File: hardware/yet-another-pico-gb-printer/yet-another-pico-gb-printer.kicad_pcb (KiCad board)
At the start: 4 copper layers, 61 x 22 mm, 90 parts, among them J1 USB_C_Receptacle_USB2.0, J2 Conn_01x02_Shielded, J3 Micro_SD_Card_Det1, J5 GameBoy_LinkPort, J6 Conn_01x03_MountingPin, J7 Conn_01x04, Q1 DMG3415U, Q2 BSS138, Q3 BSS138, Q4 BSS138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

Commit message: schematics and layout improvements
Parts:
- added C20: 100n, Capacitor_SMD:C_0402_1005Metric, F.Cu at (44.4, 81.8)
- SW2: footprint Bongo-Cat-Fidget-Toy:SW_SKRPACE010 -> yet-another-pico-gb-printer:SW-SMD_4P-L5.2-W5.2-P3.70-LS6.4
- moved Q2 25.1 mm to (42.6, 87.5), turned to -90 degrees
- moved Q3 22.8 mm to (47.8, 87.6), turned to -90 degrees
- moved R30 22.5 mm to (42.6, 84.7), turned to 180 degrees
- moved R21 22.2 mm to (50.4, 87.6), turned to -90 degrees
- moved R20 22.2 mm to (45.1, 87.5), turned to -90 degrees
- moved R22 18.9 mm to (47.8, 84.8), turned to 180 degrees
- moved R46 16.0 mm to (44.1, 98.8)
- moved R47 16.0 mm to (44.1, 101.7)
- moved D2 15.6 mm to (67.0, 74.4)
- moved Q4 15.2 mm to (53.1, 87.7), turned to -90 degrees
- moved R24 14.1 mm to (55.6, 87.7), turned to -90 degrees
- moved R23 11.8 mm to (53.1, 84.9), turned to 180 degrees
- moved SW2 9.22 mm to (67.0, 80.2)
- moved SW5 8.80 mm to (35.7, 88.5)
- moved R14 5.46 mm to (54.2, 72.6)
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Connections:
- SW5 pad 4: unconnected-(SW5-A-Pad4) -> /~{USB_BOOT}
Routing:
- net +3V3: track 29.0 -> 124.3 mm, vias 0 -> 9
- net /GB_SO: track 0.00 -> 36.8 mm
- net /GB_SC: track 0.00 -> 36.7 mm
- net /GB_SI: track 0.00 -> 27.2 mm
- net Net-(SW3-C): track 1.53 -> 24.7 mm, vias 0 -> 1
- net /SPI_1_MISO: track 0.00 -> 12.7 mm, vias 0 -> 1
- net /SPI_1_MOSI: track 0.00 -> 10.9 mm, vias 0 -> 1
- net /GB_SCK: track 0.00 -> 9.46 mm
- net /SPI_1_SCK: track 0.00 -> 8.71 mm, vias 0 -> 1
- net /GB_MOSI: track 0.00 -> 8.46 mm
- net /PUSH_BTN: track 0.00 -> 8.35 mm
- net /SPI_1_CS: track 0.00 -> 7.70 mm, vias 0 -> 1
- net +BATT: track 21.9 -> 29.1 mm
- net /GB_MISO: track 0.00 -> 6.35 mm
- net 3V3: track 0.00 -> 6.00 mm
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
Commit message: schematics and layout improvements
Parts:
- added H1: M2, MountingHole:MountingHole_2.2mm_M2_Pad, F.Cu at (74.8, 71.9)
- added H2: M2, MountingHole:MountingHole_2.2mm_M2_Pad, F.Cu at (74.7, 88.4)
- added H3: M2, MountingHole:MountingHole_2.2mm_M2_Pad, F.Cu at (0.58, 86.9)
- added H4: M2, MountingHole:MountingHole_2.2mm_M2_Pad, F.Cu at (41.8, 88.3)

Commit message: sent to fab
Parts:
- removed H1, H2, H3, H4: M2, MountingHole:MountingHole_2.2mm_M2_Pad
- removed R25: 10k, Resistor_SMD:R_0603_1608Metric
- added R15: 0, Resistor_SMD:R_0402_1005Metric, F.Cu at (68.2, 86.1)
- added R16: 0, Resistor_SMD:R_0402_1005Metric, F.Cu at (68.2, 85.1)
- added R17: 0, Resistor_SMD:R_0402_1005Metric, F.Cu at (68.1, 87.1)
- added R18: 0, Resistor_SMD:R_0402_1005Metric, F.Cu at (68.1, 88.1)
- added R19: 10k, Resistor_SMD:R_0402_1005Metric, F.Cu at (66.0, 85.6)
- J5: footprint Gekkio_Connector:GameBoy_LinkPort_MGB_Horizontal -> yet-another-pico-gb-printer:GBA-LINK
- J6: moved to B.Cu
- R20, R21, R22, R23, R24, R26, R29, R3, R30: footprint Resistor_SMD:R_0603_1608Metric -> Resistor_SMD:R_0402_1005Metric
- SW3: footprint Bongo-Cat-Fidget-Toy:SW-SMD_SK-3245S-L1-A-1 -> yet-another-pico-gb-printer:SW-SMD_K3-1280S-L1
- moved J6 37.2 mm to (62.2, 90.2)
- moved R42 32.3 mm to (64.1, 85.1)
- moved R41 32.3 mm to (64.1, 86.1)
- moved R10 23.2 mm to (41.0, 87.5), turned to 90 degrees
- moved R47 21.8 mm to (56.2, 83.6)
- moved D3 21.3 mm to (39.7, 87.6), turned to 90 degrees
- moved R46 18.3 mm to (56.2, 85.1)
- moved SW3 6.61 mm to (28.1, 74.4), turned to 90 degrees
- moved C25 4.25 mm to (29.6, 84.8), turned to 180 degrees
- moved J5 3.55 mm to (70.5, 80.2), turned to 90 degrees
- moved J3 3.10 mm to (51.6, 85.7)
- moved D2 1.94 mm to (65.0, 74.6), turned to 180 degrees
- moved SW2 1.93 mm to (65.1, 80.1)
- moved SW5 0.98 mm to (35.6, 87.5)
- moved J1 0.92 mm to (19.2, 80.2)
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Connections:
- net Net-(U1-USB_DM) renamed /PICO_USB_D_N
- net Net-(U1-USB_DP) renamed /PICO_USB_D_P
- D2 pad 4: 3V3 -> +3V3
- J5 pad 2: /GB_SO -> Net-(J5-SO)
- J5 pad 3: /GB_SI -> Net-(J5-SI)
- R32 pad 1: Net-(SW3-C) -> Net-(SW3-A)
- R4 pad 1: Net-(SW3-C) -> Net-(SW3-A)
- SW2 pad 3: 3V3 -> +3V3
- SW2 pad 4: 3V3 -> +3V3
- SW3 pad 1: Net-(SW3-C) -> unconnected-(SW3-C-Pad1)
- SW3 pad 3: unconnected-(SW3-A-Pad3) -> Net-(SW3-A)
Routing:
- net +3V3: track 124.3 -> 164.6 mm
- net +5V: track 0.00 -> 38.1 mm, vias 0 -> 3
- net Net-(U1-SWCLK): track 17.3 -> 44.3 mm
- net Net-(SW3-C): track 24.7 -> 0.00 mm, vias 1 -> 0
- net /RUN: track 10.9 -> 35.2 mm, vias 1 -> 2
- net /OLED_SDA: track 0.00 -> 21.2 mm, vias 0 -> 2
- net /OLED_SCL: track 0.00 -> 19.9 mm, vias 0 -> 2
- net /PUSH_BTN: track 8.35 -> 27.2 mm, vias 0 -> 2
- net /LED0: track 0.00 -> 16.3 mm, vias 0 -> 2
- net Net-(J5-SO): track 0.00 -> 14.0 mm
- net Net-(U1-SWD): track 20.6 -> 33.1 mm
- net /GB_SO: track 36.8 -> 24.7 mm
- net /SD_DET: track 0.00 -> 11.8 mm, vias 0 -> 1
- net Net-(J5-SI): track 0.00 -> 11.4 mm
- net GND: track 0.00 -> 10.1 mm, vias 0 -> 45
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- added copper zone on B.Cu, net GND
- added copper zone on F.Cu, net GND
- added copper zone on In1.Cu, net GND
- added copper zone on In2.Cu, net GND
- added copper zone on B.Cu, net Net-(U4-EN)
- added copper zone on B.Cu, net Net-(U4-VOUT)
- added copper zone on B.Cu, net Net-(U6-EN)
- added copper zone on B.Cu, net Net-(U6-VOUT)
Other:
- board size 61 x 22 mm -> 61 x 26 mm
- board text added: "AM 2k24"
- board text added: "BOOT"
- board text added: "RST"
- board text added: "yet another gb pico printer"

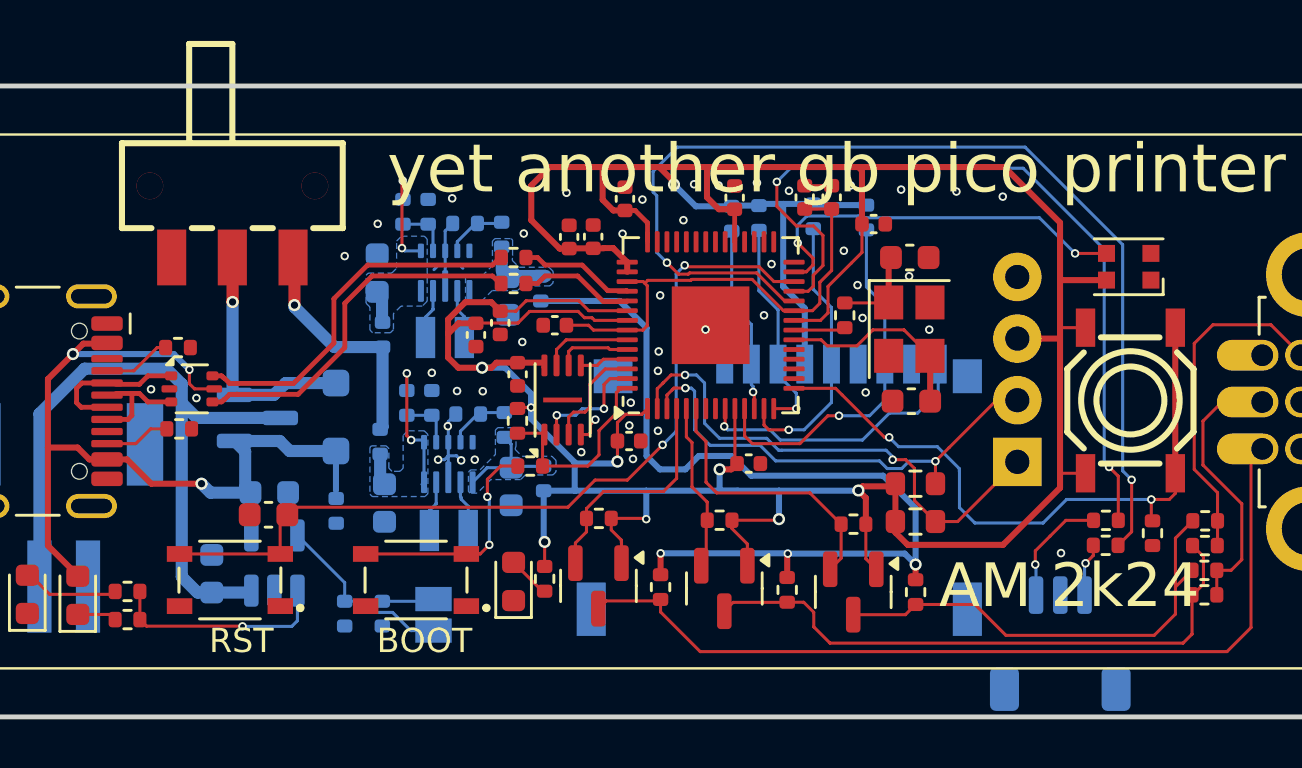
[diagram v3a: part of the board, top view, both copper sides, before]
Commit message: minor changes for jlc
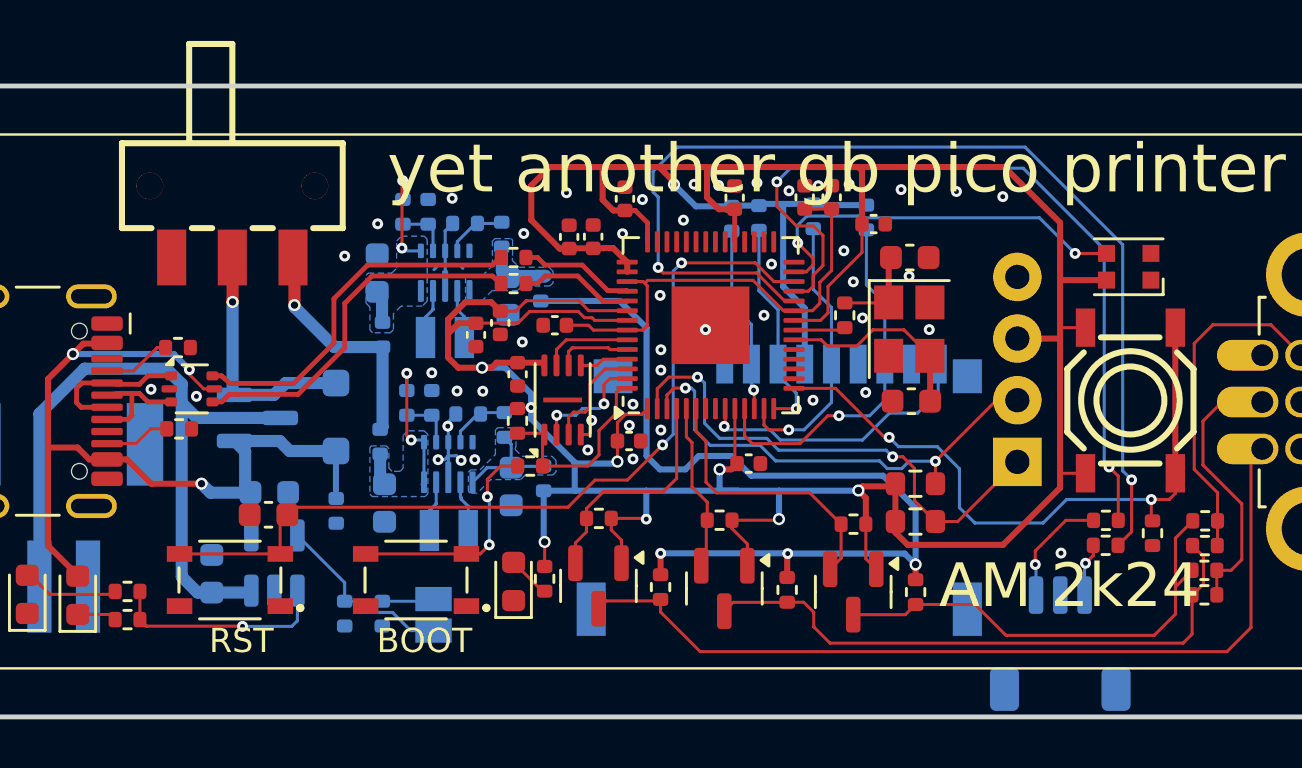
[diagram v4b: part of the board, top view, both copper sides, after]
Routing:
- net GND: track 10.1 -> 10.0 mm, vias 45 -> 47
